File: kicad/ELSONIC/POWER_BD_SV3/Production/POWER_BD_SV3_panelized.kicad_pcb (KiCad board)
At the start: 2 copper layers, 150 x 98 mm, 99 parts, among them J2 SMW250-06P, J3 SMW250-02P, T1 EI2811BP, T2 EER28, U1 ICE3BR0665J, U2 H11AA1, U3 PC817, U4 ATTINY85-20PU_1, U5 MOC3021M, U6 LM7805_TO220

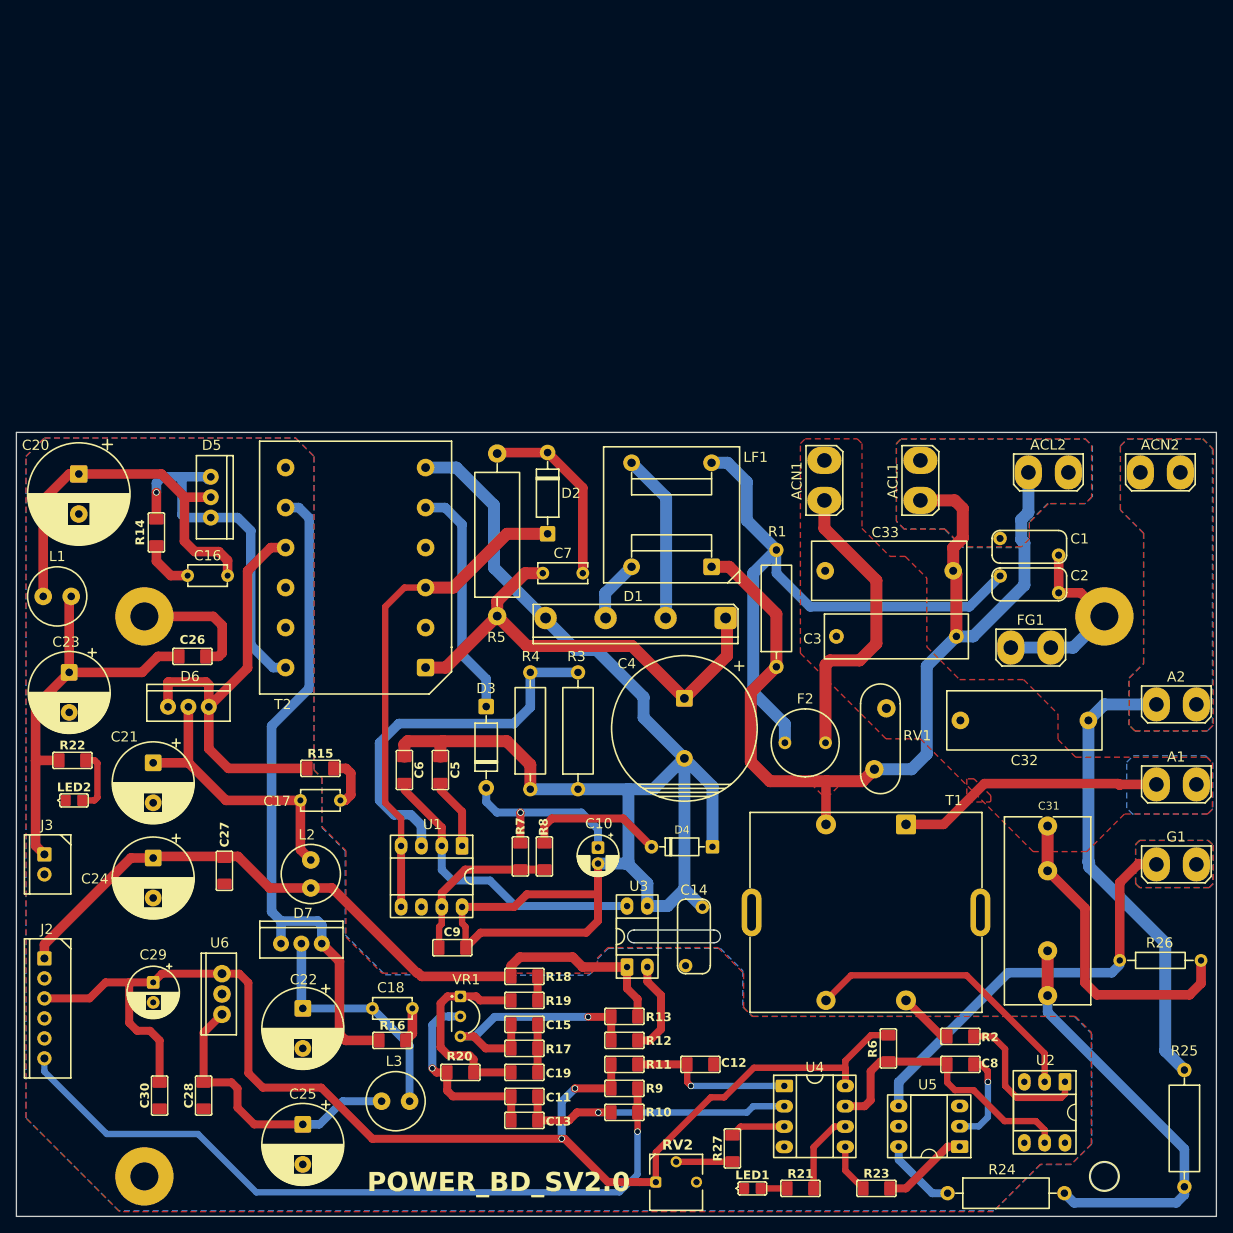
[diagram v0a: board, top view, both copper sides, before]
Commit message: Updated dimmer settings and final adjustments made.
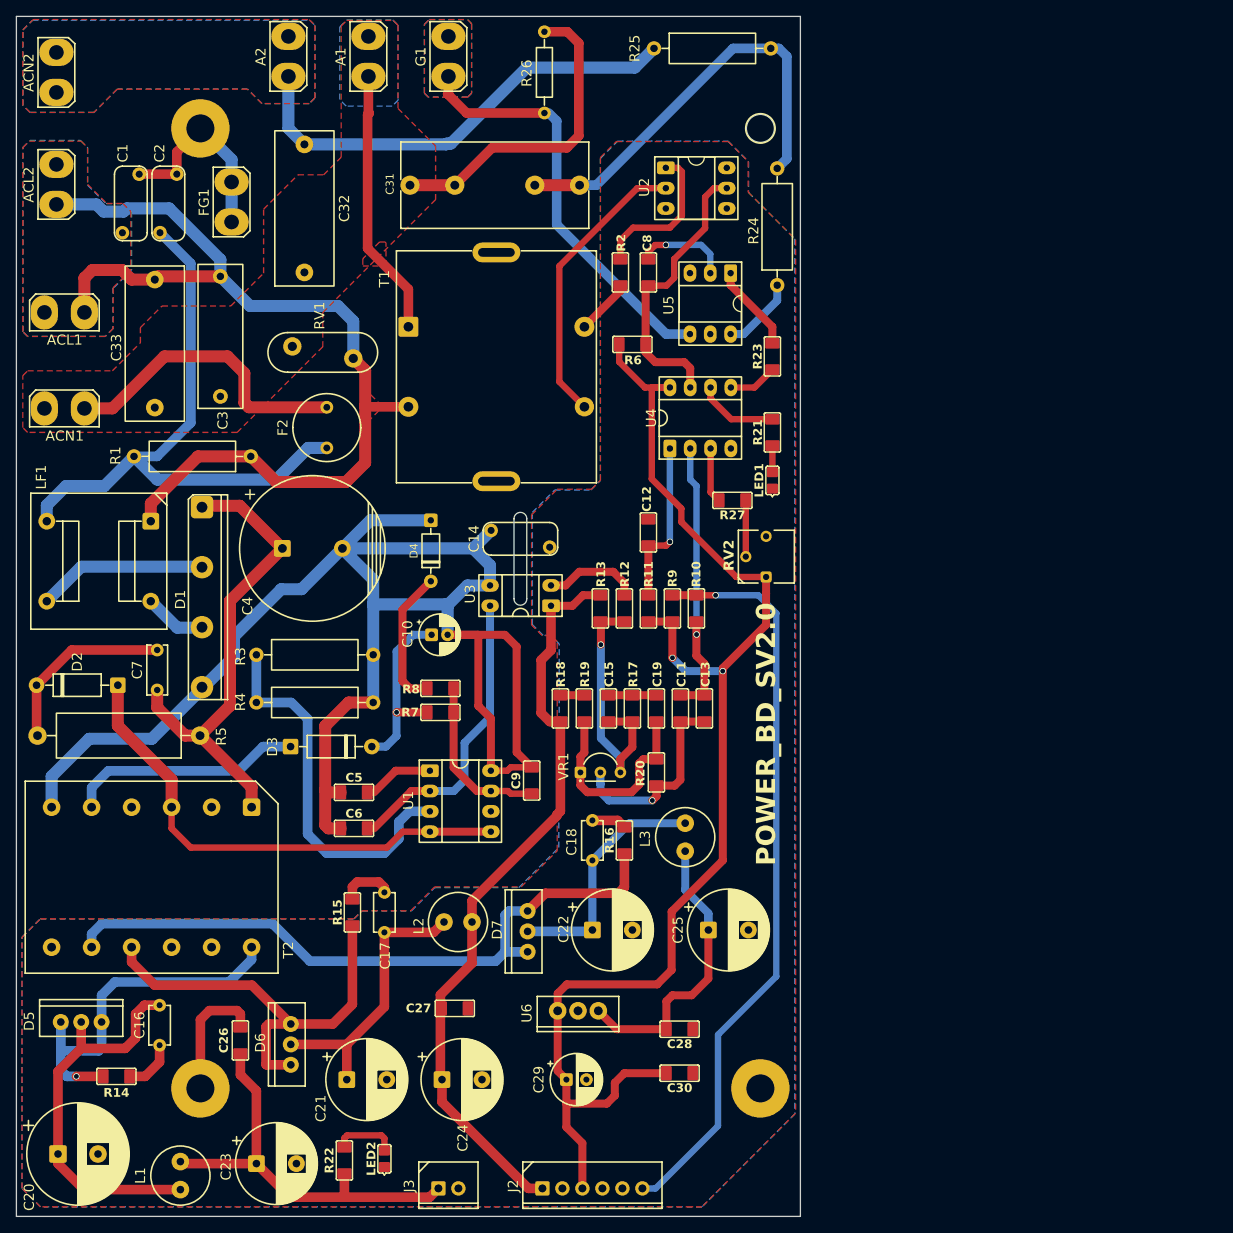
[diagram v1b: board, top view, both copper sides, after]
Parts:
- moved R25 147.3 mm to (87.0, -146.0), turned to 0 degrees
- moved ACN2 146.8 mm to (5.00, -143.0), turned to 90 degrees
- moved H4 137.9 mm to (93.0, -136.0), turned to 90 degrees
- moved A2 137.4 mm to (34.0, -145.0), turned to 90 degrees
- moved A1 135.9 mm to (44.0, -145.0), turned to 90 degrees
- moved G1 135.9 mm to (54.0, -145.0), turned to 90 degrees
- moved R26 135.1 mm to (66.0, -143.0), turned to 90 degrees
- moved ACL2 129.1 mm to (5.00, -129.0), turned to 90 degrees
- moved H1 128.4 mm to (23.0, -136.0), turned to 90 degrees
- moved R24 124.1 mm to (95.1, -123.7), turned to 90 degrees
- moved U2 123.5 mm to (85.0, -128.5), turned to 0 degrees
- moved C1 120.2 mm to (14.3, -126.6), turned to 90 degrees
- moved C2 117.7 mm to (19.0, -126.6), turned to -90 degrees
- moved FG1 114.4 mm to (26.9, -126.8), turned to 90 degrees
- moved C31 114.0 mm to (59.8, -128.9), turned to 180 degrees
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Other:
- board size 150 x 98 mm -> 98 x 150 mm
